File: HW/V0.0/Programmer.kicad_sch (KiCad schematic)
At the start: 37 parts, among them J4 PG ICSP, Q5 SI2302, Q6 SI2302, Q7 SI2302, U11 PIC32MM0064GPM028, U6 SN74LVC1T45, U7 SN74LVC1T45, U8 SN74LVC1T45, U9 SN74LVC1T45

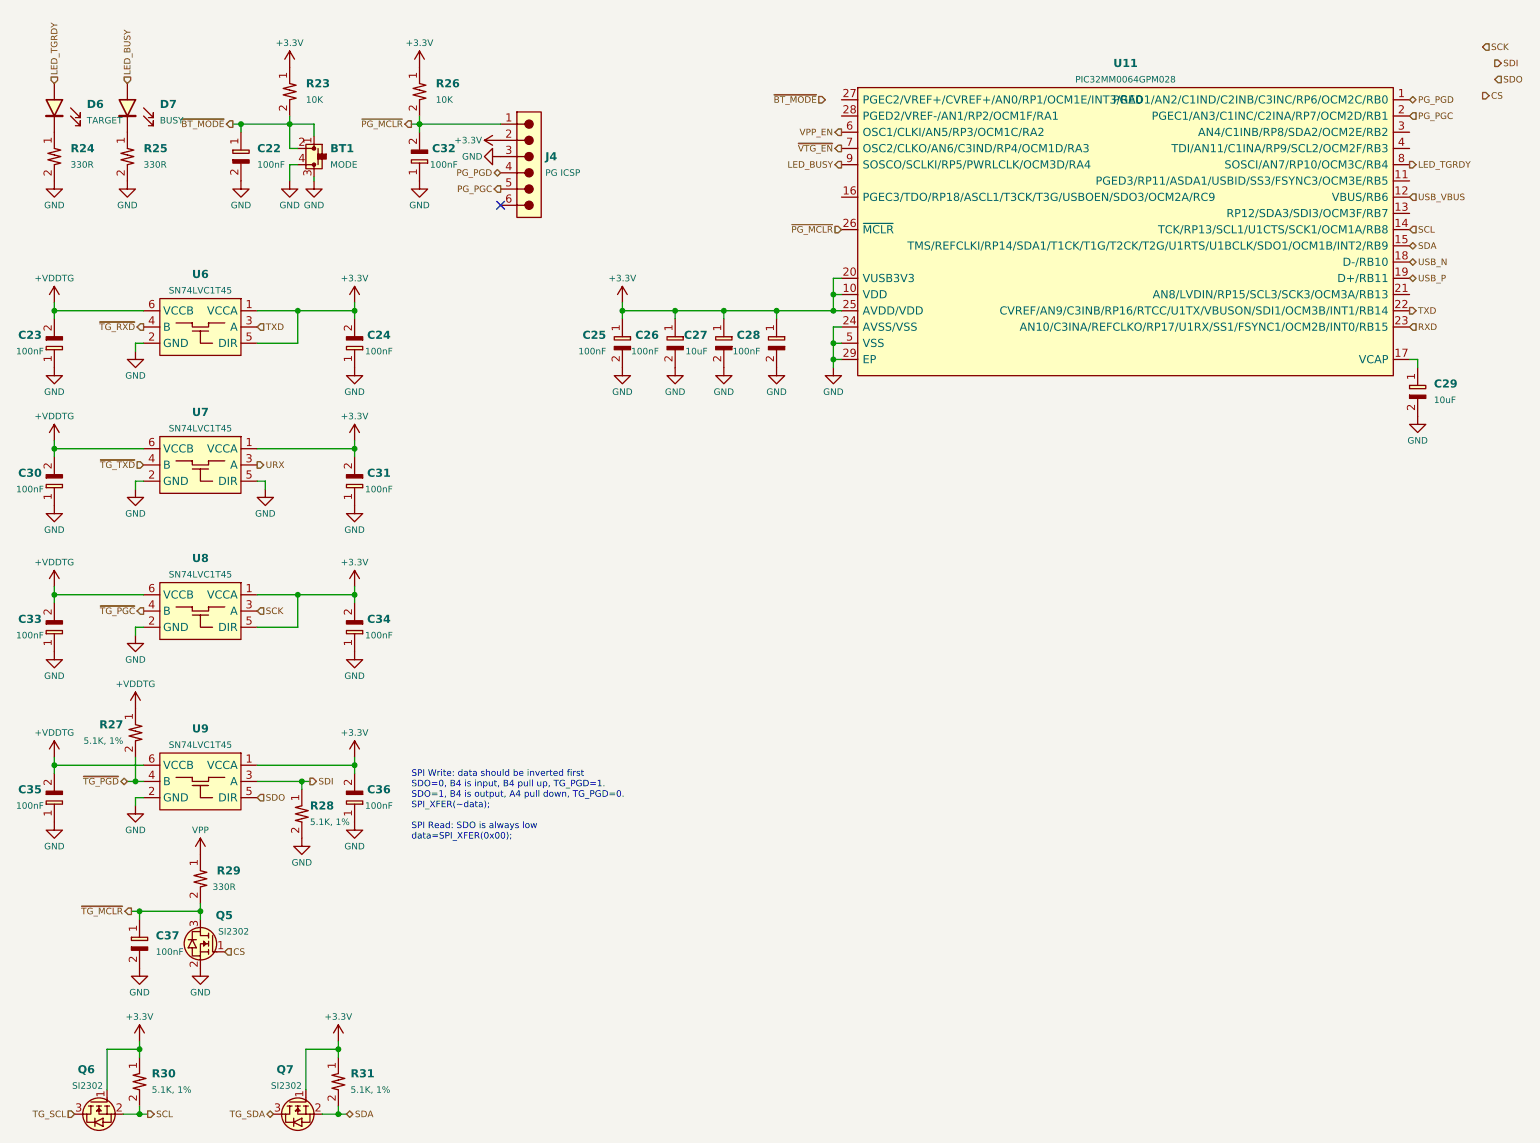
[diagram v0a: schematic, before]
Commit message: PIC16-DevKit-PCB-877 layout update 2
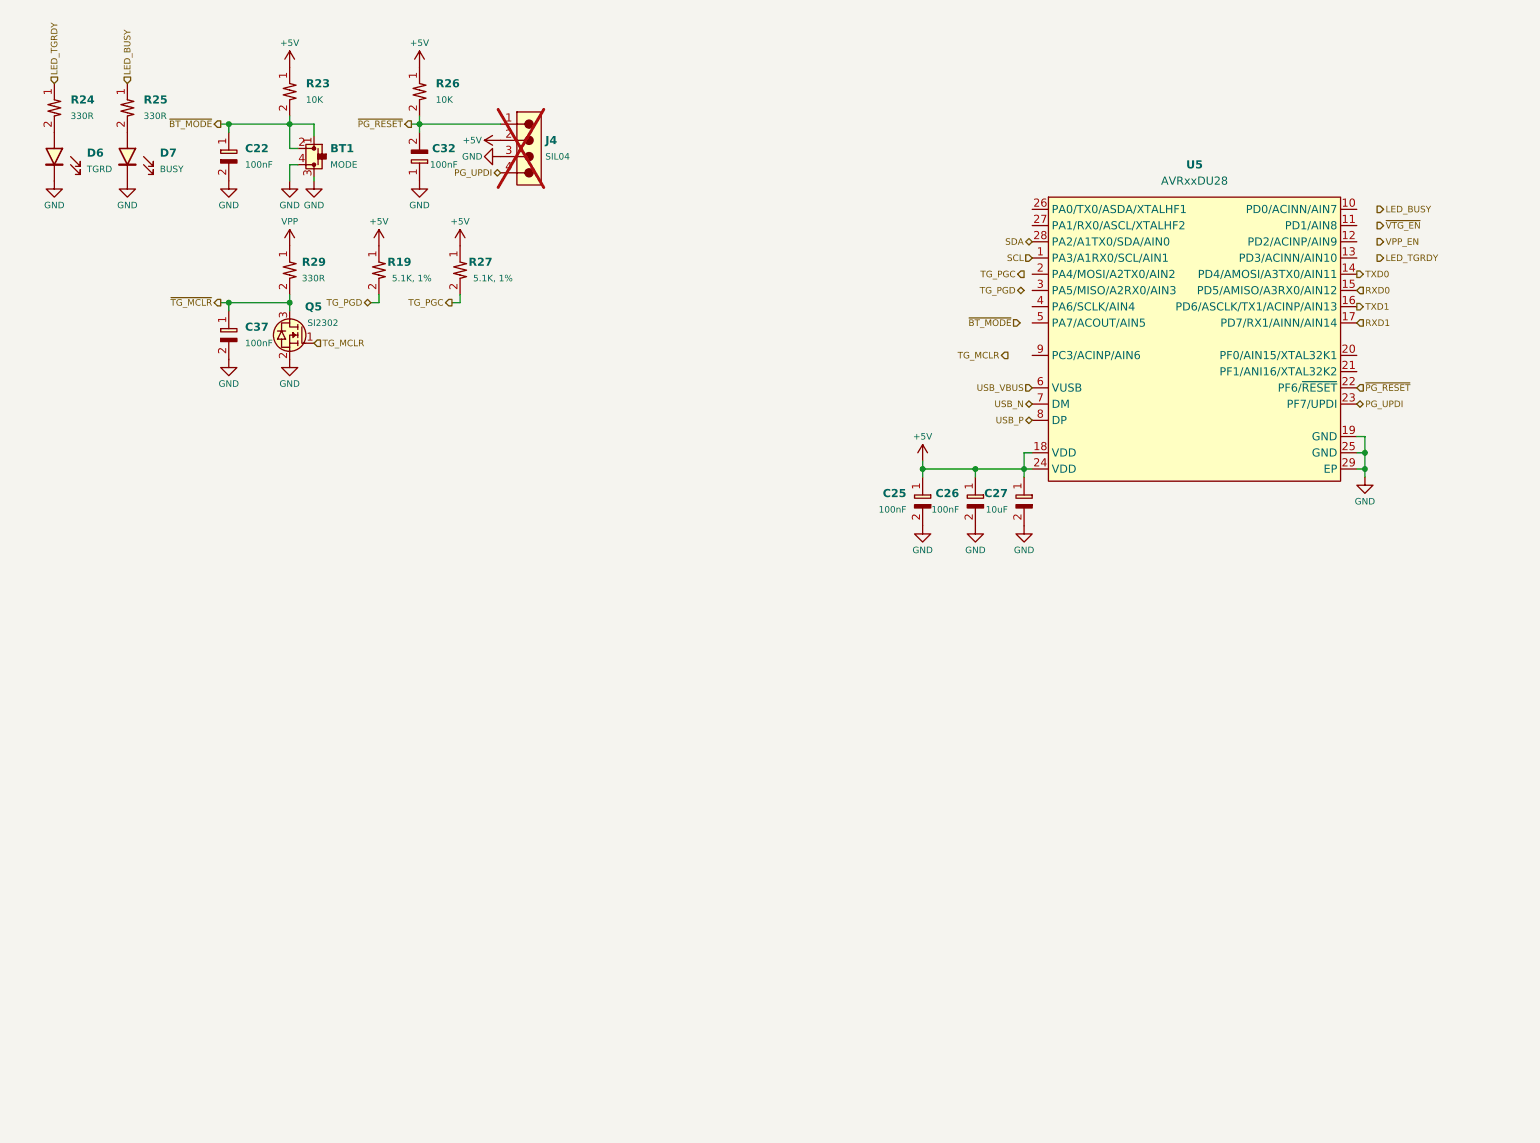
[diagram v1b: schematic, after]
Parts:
- removed C23, C24, C28, C30, C31, C33, C34, C35, C36: 100nF, SAMPI:CAP0603, symbol Triet_KiCAD_Sym:CAP_CER
- removed C29: 10uF, SAMPI:CAP0603, symbol Triet_KiCAD_Sym:CAP_CER
- removed J4: PG ICSP, SAMPI:HD-1x6x1.27MM-TH, symbol SAMPI:SIL06
- removed Q6, Q7: SI2302, SAMPI:SOT23, symbol SAMPI:FET_N-CH
- removed R28, R30, R31: 5.1K, 1%, SAMPI:RES0603, symbol Triet_KiCAD_Sym:RES
- removed U11: PIC32MM0064GPM028, SAMPI:UQFN28-4x4-EP, symbol SAMPI:PIC32MM0256GPM028-I_M6
- removed U6, U7, U8, U9: SN74LVC1T45, SAMPI:SOT-23-6_MCHP, symbol SAMPI:LEVEL_SHIFT_1CH
- added J4: SIL04, SAMPI:HD-1x4x1.27MM-TH, symbol SAMPI:SIL04-1
- added R19: 5.1K, 1%, SAMPI:RES0603, symbol Triet_KiCAD_Sym:RES
- added U5: AVRxxDU28, SAMPI:VQFN28-4x4-EP, symbol SAMPI:AVRxxDU28
- D6: value TARGET -> TGRD
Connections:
- net +VDDTG is gone; now on net +5V: R27.1
- net GND: now also D6.K, D7.K, J4.3, U5.19 (GND), U5.25 (GND), U5.29 (EP); no longer R24.2, R25.2
- net LED_BUSY: now also R25.1; no longer D7.A
- net LED_TGRDY: now also R24.1; no longer D6.A
- net SCL: now also U5.1 (PA3/A1RX0/SCL/AIN1)
- net SDA: now also U5.28 (PA2/A1TX0/SDA/AIN0)
- net USB_N: now also U5.7 (DM)
- net USB_P: now also U5.8 (DP)
- net USB_VBUS: now also U5.6 (VUSB)
- net +3.3V renamed +5V
- net +5V: now also J4.2, R19.1, U5.18 (VDD), U5.24 (VDD)
- net CS renamed TG_MCLR
- net ~{PG_MCLR} renamed ~{PG_RESET}
- net ~{PG_RESET}: now also J4.1, U5.22 (PF6/~{RESET})
- net ~{TG_PGD} renamed TG_PGC
- new net: D7.A, R25.2
- new net: D6.A, R24.2
- new net PG_UPDI: J4.4, U5.23 (PF7/UPDI)
- new net RXD0: U5.15 (PD5/AMISO/A3RX0/AIN12)
- new net RXD1: U5.17 (PD7/RX1/AINN/AIN14)
- new net TG_PGD: R19.2
- new net TXD0: U5.14 (PD4/AMOSI/A3TX0/AIN11)
- new net TXD1: U5.16 (PD6/ASCLK/TX1/ACINP/AIN13)
- no-connect marks 1 -> 0
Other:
- note removed: "SPI Write: data should be inverted first SDO=0, B4 is input, B4 pull up, TG_PGD=1. SDO=1, B4 is output, A4 pull down, TG_PGD=0. SPI_XFER(~data); SPI Read: SDO is always low data=SPI_XFER(0x00);"
- moved on the sheet: C22, C25, C26, C27, C37, D6, D7, Q5, R24, R25, R29

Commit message: PIC16-DevKit-PCB-877 layout update 1
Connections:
- net LED_BUSY: now also U5.3 (PA5/MISO/A2RX0/AIN3)
- net LED_TGRDY: now also U5.2 (PA4/MOSI/A2TX0/AIN2)
- net TG_MCLR: now also U5.13 (PD3/ACINN/AIN10)
- net TG_PGC: now also R19.2, U5.26 (PA0/TX0/ASDA/XTALHF1); no longer R27.2
- net TG_PGD: now also R27.2, U5.27 (PA1/RX0/ASCL/XTALHF2); no longer R19.2
- net VPP_EN: now also U5.21 (PF1/ANI16/XTAL32K2)
- net ~{BT_MODE}: now also U5.5 (PA7/ACOUT/AIN5)
- net ~{VTG_EN}: now also U5.20 (PF0/AIN15/XTAL32K1)
- no-connect marks 0 -> 5
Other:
- moved on the sheet: R19, R27
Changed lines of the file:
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@@
 		(color 0 0 0 0)
 	)
-	(wire
-		(pts
-			(xy 55.88 34.29) (xy 55.88 36.83)
-		)
-		(stroke
-			(width 0)
-			(type default)
-		)
+	(no_connect
+		(at 172.085 64.135)
 	)
-	(wire
-		(pts
-			(xy 46.355 55.88) (xy 45.085 55.88)
-		)
-		(stroke
-			(width 0)
-			(type default)
-		)
+	(no_connect
+		(at 222.885 43.815)
+	)
+	(no_connect
+		(at 172.085 56.515)
+	)
+	(no_connect
+		(at 222.885 41.275)
+	)
+	(no_connect
+		(at 222.885 46.355)
 	)
 	(wire
 		(pts
-			(xy 69.85 55.88) (xy 69.85 54.61)
+			(xy 55.88 34.29) (xy 55.88 36.83)
 		)
 		(stroke
@@
 	(wire
 		(pts
-			(xy 81.28 55.88) (xy 82.55 55.88)
+			(xy 46.355 55.88) (xy 45.085 55.88)
 		)
 		(stroke
@@
 	(wire
 		(pts
-			(xy 68.58 55.88) (xy 69.85 55.88)
-		)
-		(stroke
-			(width 0)
-			(type default)
-		)
-	)
-	(wire
-		(pts
-			(xy 82.55 54.61) (xy 82.55 55.88)
-		)
-		(stroke
-			(width 0)
-			(type default)
-		)
-	)
-	(wire
-		(pts
 			(xy 170.815 79.375) (xy 172.085 79.375)
 		)
@@
 	(hierarchical_label "TG_PGD"
 		(shape bidirectional)
-		(at 68.58 55.88 180)
+		(at 76.2 54.61 270)
 		(fields_autoplaced yes)
 		(effects
@@
 	(hierarchical_label "TG_PGC"
 		(shape output)
-		(at 170.815 51.435 180)
+		(at 172.085 41.275 180)
 		(fields_autoplaced yes)
 		(effects
@@
 	(hierarchical_label "TG_PGD"
 		(shape bidirectional)
-		(at 170.815 53.975 180)
+		(at 172.085 43.815 180)
 		(fields_autoplaced yes)
 		(effects
@@
 	(hierarchical_label "~{VTG_EN}"
 		(shape output)
-		(at 226.06 43.815 0)
+		(at 222.885 64.135 0)
 		(fields_autoplaced yes)
 		(effects
@@
 	(hierarchical_label "VPP_EN"
 		(shape output)
-		(at 226.06 46.355 0)
+		(at 222.885 66.675 0)
 		(fields_autoplaced yes)
 		(effects
@@
 	(hierarchical_label "TG_PGC"
 		(shape output)
-		(at 81.28 55.88 180)
+		(at 79.375 54.61 270)
 		(fields_autoplaced yes)
 		(effects
@@
 	(hierarchical_label "TG_MCLR"
 		(shape output)
-		(at 168.275 64.135 180)
+		(at 222.885 48.895 0)
 		(fields_autoplaced yes)
 		(effects
@@
 				(size 1.016 1.016)
 			)
-			(justify right)
+			(justify left)
 		)
 	)
 	(hierarchical_label "LED_BUSY"
 		(shape output)
-		(at 226.06 41.275 0)
+		(at 172.085 53.975 180)
 		(fields_autoplaced yes)
 		(effects
@@
 				(size 1.016 1.016)
 			)
-			(justify left)
+			(justify right)
 		)
 	)
 	(hierarchical_label "~{BT_MODE}"
 		(shape input)
-		(at 170.18 59.055 180)
+		(at 172.085 59.055 180)
 		(fields_autoplaced yes)
 		(effects
@@
 	(hierarchical_label "LED_TGRDY"
 		(shape output)
-		(at 226.06 48.895 0)
+		(at 172.085 51.435 180)
 		(fields_autoplaced yes)
 		(effects
@@
 				(size 1.016 1.016)
 			)
-			(justify left)
+			(justify right)
 		)
 	)
@@
 		(lib_name "+5V_1")
 		(lib_id "power:+5V")
-		(at 69.85 46.99 0)
-		(mirror y)
+		(at 76.2 46.99 0)
 		(unit 1)
 		(exclude_from_sim no)
@@
 		(dnp no)
 		(property "Reference" "#PWR071"
-			(at 69.85 50.8 0)
+			(at 76.2 50.8 0)
 			(effects
 				(font
@@
 		)
 		(property "Value" "+5V"
-			(at 69.85 43.18 0)
+			(at 76.2 43.18 0)
 			(effects
 				(font
@@
 		)
 		(property "Footprint" ""
-			(at 69.85 46.99 0)
+			(at 76.2 46.99 0)
 			(effects
 				(font
@@
 		)
 		(property "Datasheet" ""
-			(at 69.85 46.99 0)
+			(at 76.2 46.99 0)
 			(effects
 				(font
@@
 		)
 		(property "Description" "Power symbol creates a global label with name \"+5V\""
-			(at 69.85 46.99 0)
+			(at 76.2 46.99 0)
 			(effects
 				(font
@@
 		(on_board yes)
 		(dnp no)
-		(fields_autoplaced yes)
 		(property "Reference" "U5"
 			(at 197.485 34.29 0)
@@
 		)
 		(instances
-			(project ""
+			(project "PIC16DevKit"
 				(path "/17281b91-3f9a-4e36-96b2-66002b412b3a/6fab4358-8edb-4c81-8f5e-6901c5551004"
 					(reference "U5")
@@
 	(symbol
 		(lib_id "Triet_KiCAD_Sym:RES")
-		(at 82.55 50.8 0)
+		(at 76.2 50.8 0)
+		(mirror y)
 		(unit 1)
 		(exclude_from_sim no)
@@
 		(dnp no)
 		(property "Reference" "R27"
-			(at 87.63 49.53 0)
+			(at 71.12 49.53 0)
 			(effects
 				(font
@@
 		)
 		(property "Value" "5.1K, 1%"
-			(at 90.805 52.07 0)
+			(at 67.945 52.07 0)
 			(effects
 				(font
@@
 		)
 		(property "Footprint" "SAMPI:RES0603"
-			(at 82.55 51.054 90)
+			(at 76.2 51.054 90)
 			(effects
 				(font
@@
 		)
 		(property "Datasheet" ""
-			(at 82.55 51.054 90)
+			(at 76.2 51.054 90)
 			(effects
 				(font
@@
 		)
 		(property "Description" "RES 5.1K OHM 1% 1/10W 0603"
-			(at 93.98 50.8 0)
+			(at 64.77 50.8 0)
 			(effects
 				(font
@@
 		)
 		(property "MFT" "Yageo"
-			(at 82.55 50.8 0)
+			(at 76.2 50.8 0)
 			(effects
 				(font
@@
 		)
 		(property "MNP" "RC0603FR-075K1L"
-			(at 82.55 50.8 0)
+			(at 76.2 50.8 0)
 			(effects
 				(font
@@
 		(lib_name "+5V_1")
 		(lib_id "power:+5V")
-		(at 82.55 46.99 0)
+		(at 79.375 46.99 0)
 		(mirror y)
 		(unit 1)
@@
 		(dnp no)
 		(property "Reference" "#PWR073"
-			(at 82.55 50.8 0)
+			(at 79.375 50.8 0)
 			(effects
 				(font
@@
 		)
 		(property "Value" "+5V"
-			(at 82.55 43.18 0)
+			(at 79.375 43.18 0)
 			(effects
 				(font
@@
 		)
 		(property "Footprint" ""
-			(at 82.55 46.99 0)
+			(at 79.375 46.99 0)
 			(effects
 				(font
@@
 		)
 		(property "Datasheet" ""
-			(at 82.55 46.99 0)
+			(at 79.375 46.99 0)
 			(effects
 				(font
@@
 		)
 		(property "Description" "Power symbol creates a global label with name \"+5V\""
-			(at 82.55 46.99 0)
+			(at 79.375 46.99 0)
 			(effects
 				(font
@@
 	(symbol
 		(lib_id "Triet_KiCAD_Sym:RES")
-		(at 69.85 50.8 0)
+		(at 79.375 50.8 0)
 		(unit 1)
 		(exclude_from_sim no)
@@
 		(dnp no)
 		(property "Reference" "R19"
-			(at 74.93 49.53 0)
+			(at 84.455 49.53 0)
 			(effects
 				(font
@@
 		)
 		(property "Value" "5.1K, 1%"
-			(at 78.105 52.07 0)
+			(at 87.63 52.07 0)
 			(effects
 				(font
@@
 		)
 		(property "Footprint" "SAMPI:RES0603"
-			(at 69.85 51.054 90)
+			(at 79.375 51.054 90)
 			(effects
 				(font
@@
 		)
 		(property "Datasheet" ""
-			(at 69.85 51.054 90)
+			(at 79.375 51.054 90)
 			(effects
 				(font
@@
 		)
 		(property "Description" "RES 5.1K OHM 1% 1/10W 0603"
-			(at 81.28 50.8 0)
+			(at 90.805 50.8 0)
 			(effects
 				(font
@@
 		)
 		(property "MFT" "Yageo"
-			(at 69.85 50.8 0)
+			(at 79.375 50.8 0)
 			(effects
 				(font
@@
 		)
 		(property "MNP" "RC0603FR-075K1L"
-			(at 69.85 50.8 0)
+			(at 79.375 50.8 0)
 			(effects
 				(font
@@
 		)
 		(instances
-			(project ""
+			(project "PIC16DevKit"
 				(path "/17281b91-3f9a-4e36-96b2-66002b412b3a/6fab4358-8edb-4c81-8f5e-6901c5551004"
 					(reference "J4")
